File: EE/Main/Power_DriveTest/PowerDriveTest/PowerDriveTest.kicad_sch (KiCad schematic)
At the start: 31 parts, among them J8 Conn_01x02_Male, P1 USB_C_Plug_USB2.0, SW1 EG1206A, U2 LM3670MF-3.3, U4 MCP73832-2-OT, U5 MCP1640Cx-xCHY

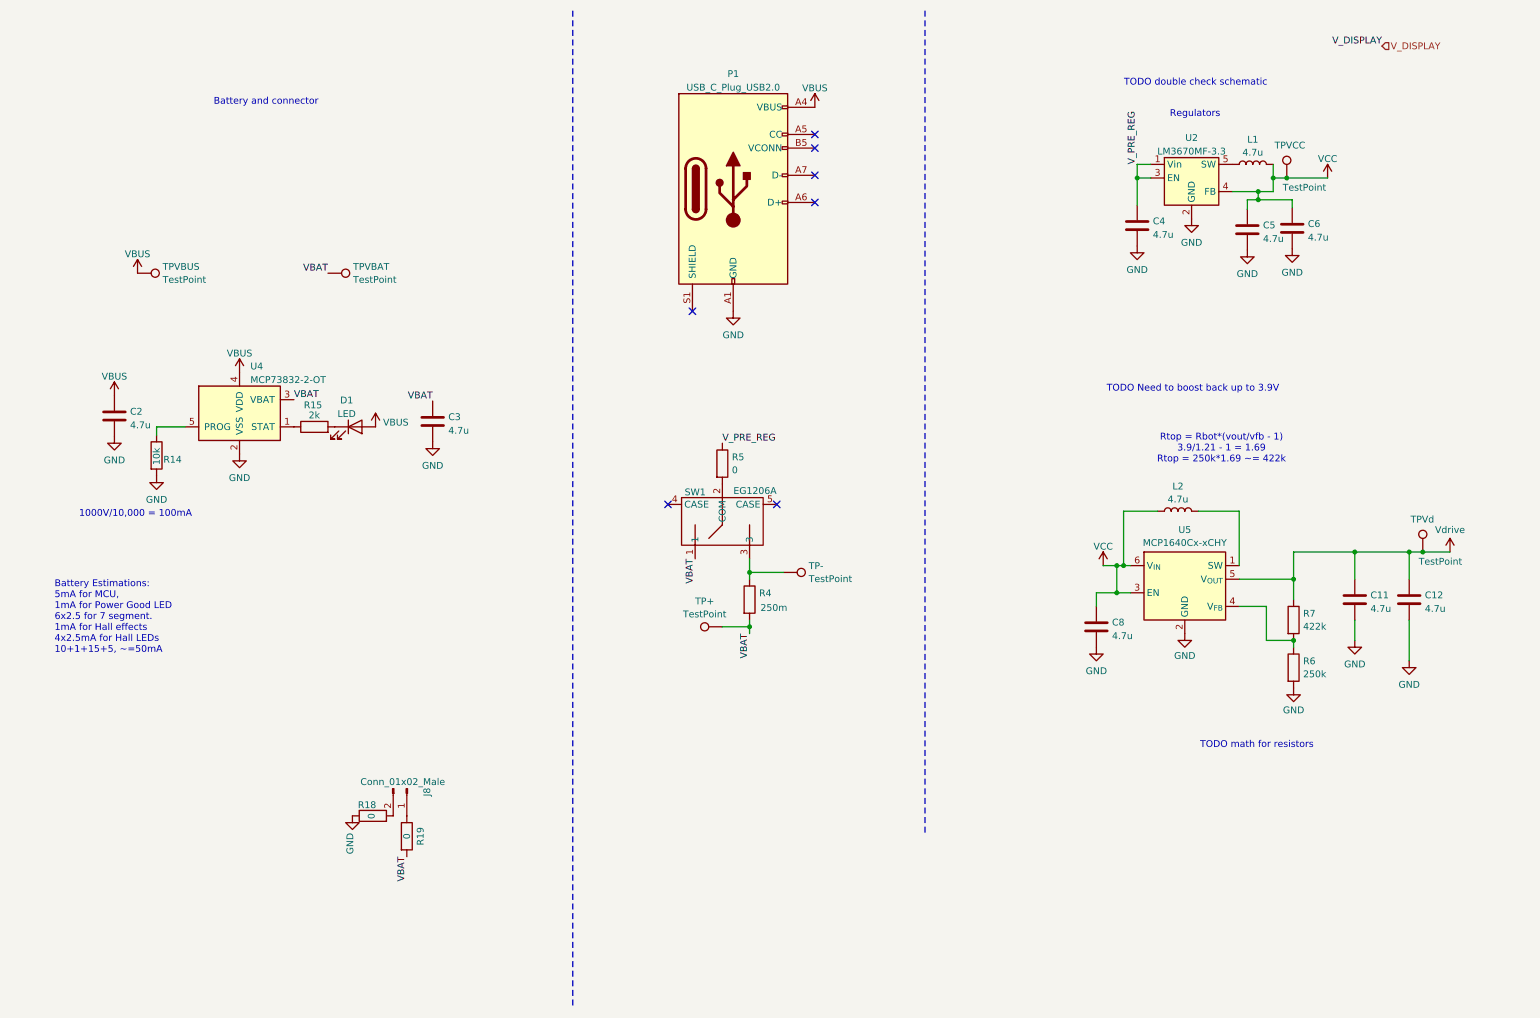
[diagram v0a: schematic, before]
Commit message: Sample Board for Power Supplies, Micro, And LED Driving.
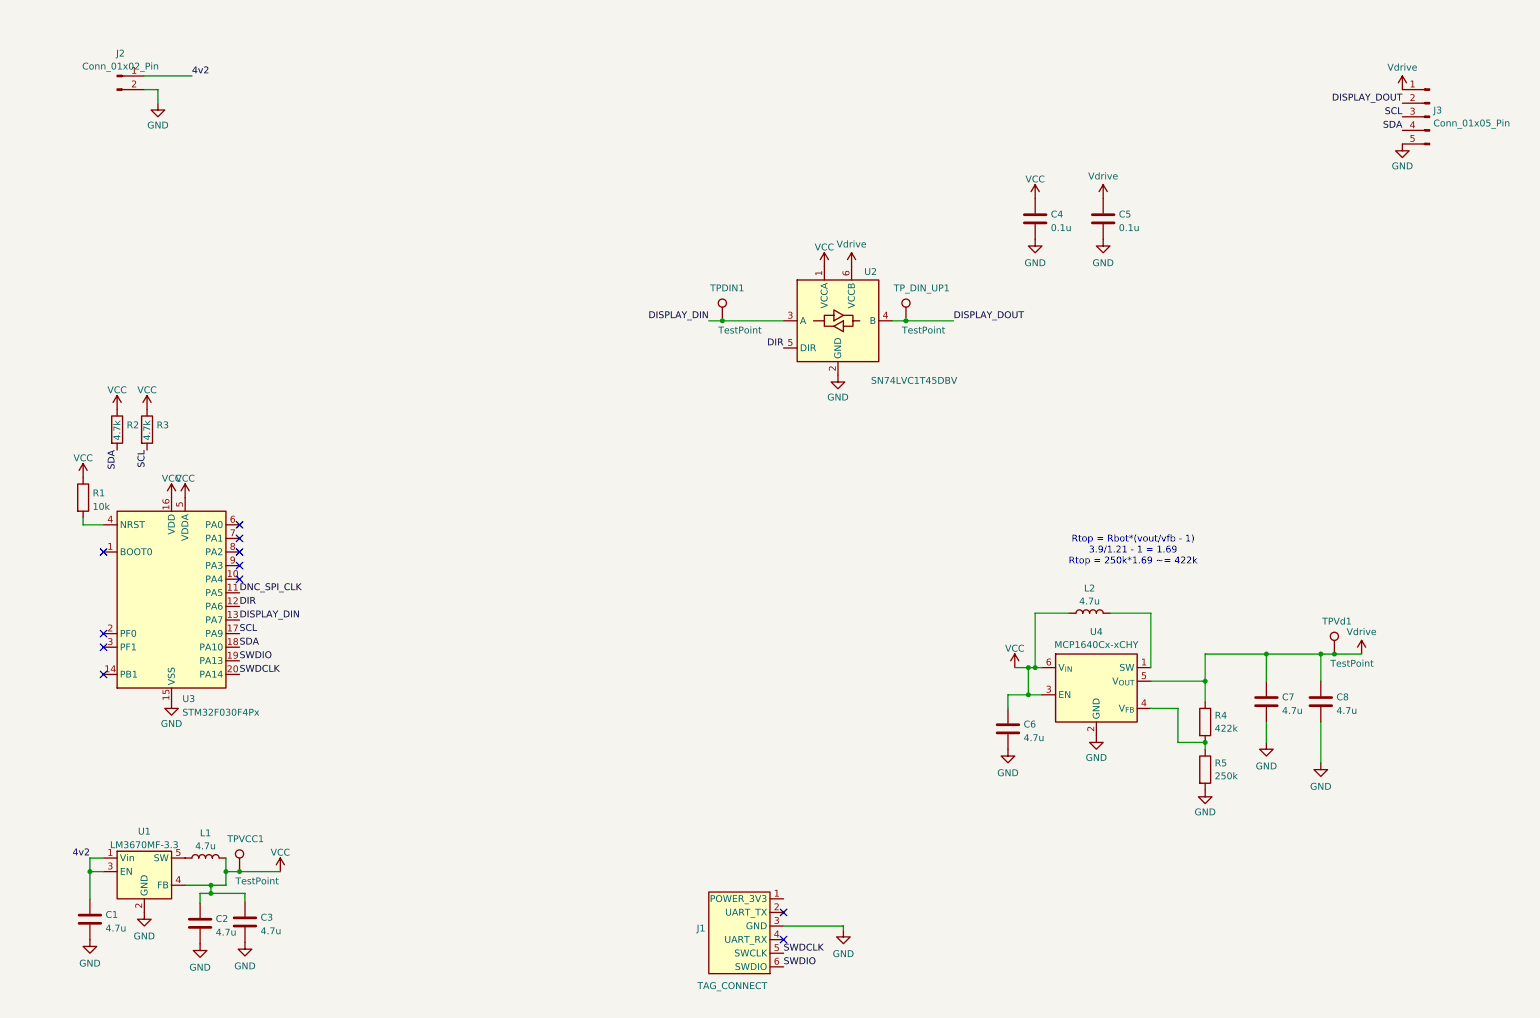
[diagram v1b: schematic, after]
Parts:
- removed C11, C12: 4.7u, Capacitor_SMD:C_0603_1608Metric, symbol Device:C
- removed D1: LED, LED_SMD:LED_0603_1608Metric, symbol Device:LED
- removed J8: Conn_01x02_Male, Connector_JST:JST_PH_B2B-PH-K_1x02_P2.00mm_Vertical, symbol Connector:Conn_01x02_Male
- removed P1: USB_C_Plug_USB2.0, Connector_USB:USB_C_Receptacle_GCT_USB4085, symbol Connector:USB_C_Plug_USB2.0
- removed R14: 10k, Resistor_SMD:R_0402_1005Metric, symbol Device:R
- removed R15: 2k, Resistor_SMD:R_0402_1005Metric, symbol Device:R
- removed R18, R19: 0, Resistor_SMD:R_0402_1005Metric, symbol Device:R
- removed R6: 250k, symbol Device:R
- removed R7: 422k, symbol Device:R
- removed SW1: EG1206A, Library:EG1206A_EWI, symbol New_Library:EG1206A
- removed TP+, TP-, TPVBAT, TPVBUS, TPVCC, TPVd: TestPoint, TestPoint:TestPoint_Pad_1.5x1.5mm, symbol Connector:TestPoint
- removed U2: LM3670MF-3.3, Package_TO_SOT_SMD:TSOT-23-5, symbol Regulator_Switching:LM3670MF
- removed U4: MCP73832-2-OT, Package_TO_SOT_SMD:SOT-23-5, symbol Battery_Management:MCP73832-2-OT
- removed U5: MCP1640Cx-xCHY, Package_TO_SOT_SMD:SOT-23-6, symbol Regulator_Switching:MCP1640Cx-xCHY
- added C1, C7: 4.7u, Capacitor_SMD:C_0603_1608Metric, symbol Device:C
- added J1: TAG_CONNECT, Connector:Tag-Connect_TC2030-IDC-FP_2x03_P1.27mm_Vertical, symbol ACTempDisconnect:TAG_CONNECT
- added J2: Conn_01x02_Pin, Connector_PinHeader_2.54mm:PinHeader_1x02_P2.54mm_Vertical, symbol Connector:Conn_01x02_Pin
- added J3: Conn_01x05_Pin, Connector_PinHeader_2.54mm:PinHeader_1x05_P2.54mm_Vertical, symbol Connector:Conn_01x05_Pin
- added R1: 10k, Resistor_SMD:R_0402_1005Metric, symbol Device:R
- added R2, R3: 4.7k, Resistor_SMD:R_0402_1005Metric, symbol Device:R
- added TPDIN1, TPVCC1, TPVd1, TP_DIN_UP1: TestPoint, TestPoint:TestPoint_Pad_1.5x1.5mm, symbol Connector:TestPoint
- added U1: LM3670MF-3.3, Package_TO_SOT_SMD:TSOT-23-5, symbol Regulator_Switching:LM3670MF
- added U2: SN74LVC1T45DBV, Package_TO_SOT_SMD:SOT-23-6, symbol Logic_LevelTranslator:SN74LVC1T45DBV
- added U3: STM32F030F4Px, Package_SO:TSSOP-20_4.4x6.5mm_P0.65mm, symbol MCU_ST_STM32F0:STM32F030F4Px
- added U4: MCP1640Cx-xCHY, Package_TO_SOT_SMD:SOT-23-6, symbol Regulator_Switching:MCP1640Cx-xCHY
- C4, C5: value 4.7u -> 0.1u; footprint Capacitor_SMD:C_0603_1608Metric -> Capacitor_SMD:C_0402_1005Metric
- R4: value 250m -> 422k; footprint Resistor_SMD:R_0805_2012Metric -> Resistor_SMD:R_0402_1005Metric_Pad0.72x0.64mm_HandSolder
- R5: value 0 -> 250k
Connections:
- net VBUS is gone; now on net VCC: C2.1
- net GND: now also R5.2, C1.2, C7.2, J1.3 (GND), J2.2 (Pin_2), J3.5 (Pin_5), U1.2 (GND), U2.2 (GND), U3.15 (VSS), U4.2 (GND)
- net VCC: now also C3.1, C4.1, R1.1, R2.1, R3.1, TPVCC1.1, U1.4 (FB), U2.1 (VCCA), U3.16 (VDD), U3.5 (VDDA), U4.3 (EN), U4.6 (V_{IN}); no longer C5.1, C8.1
- net Vdrive: now also C5.1, C8.1, R4.1, C7.1, J3.1 (Pin_1), TPVd1.1, U2.6 (VCCB), U4.5 (V_{OUT})
- net at L2.2: now also U4.1 (SW)
- net at L1.1: now also U1.5 (SW)
- net VBAT: no longer names the net of R4.2
- net VBAT: now also R5.1, U4.4 (V_{FB}); no longer C3.1
- removed net V_PRE_REG: C4.1, R5.1
- new net: R1.2, U3.4 (NRST)
- new net 4v2: C1.1, J2.1 (Pin_1), U1.1 (Vin), U1.3 (EN)
- new net DIR: U2.5 (DIR), U3.12 (PA6)
- new net DISPLAY_DIN: TPDIN1.1, U2.3 (A), U3.13 (PA7)
- new net DISPLAY_DOUT: J3.2 (Pin_2), TP_DIN_UP1.1, U2.4 (B)
- new net DNC_SPI_CLK: U3.11 (PA5)
- new net SCL: J3.3 (Pin_3), R3.2, U3.17 (PA9)
- new net SDA: J3.4 (Pin_4), R2.2, U3.18 (PA10)
- new net SWDCLK: J1.5 (SWCLK), U3.20 (PA14)
- new net SWDIO: J1.6 (SWDIO), U3.19 (PA13)
- no-connect marks 7 -> 11
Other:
- note removed: "1000V/10,000 = 100mA"
- note removed: "Battery Estimations: 5mA for MCU, 1mA for Power Good LED 6x2.5 for 7 segment. 1mA for Hall effects 4x2.5mA for Hall LEDs 10+1+15+5, ~=50mA"
- note removed: "Battery and connector"
- note removed: "Regulators"
- note removed: "TODO Need to boost back up to 3.9V"
- note removed: "TODO double check schematic"
- note removed: "TODO math for resistors"

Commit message: New Power Board off to mfging
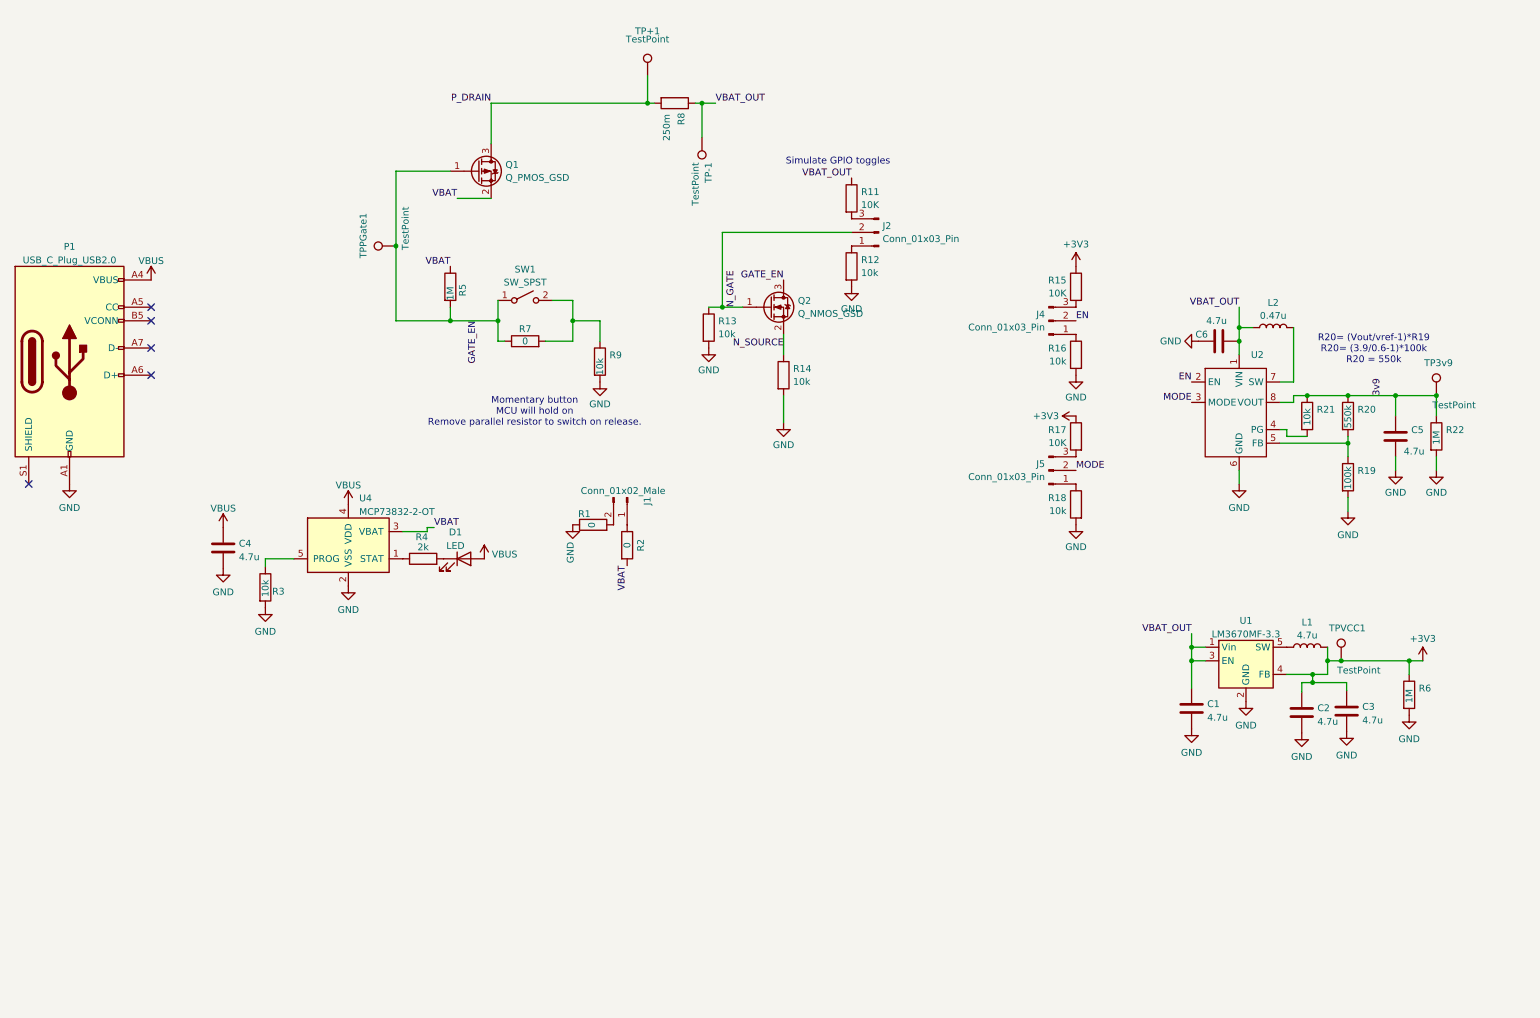
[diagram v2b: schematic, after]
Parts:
- removed C7, C8: 4.7u, Capacitor_SMD:C_0603_1608Metric, symbol Device:C
- removed J1: TAG_CONNECT, Connector:Tag-Connect_TC2030-IDC-FP_2x03_P1.27mm_Vertical, symbol ACTempDisconnect:TAG_CONNECT
- removed J2: Conn_01x02_Pin, Connector_PinHeader_2.54mm:PinHeader_1x02_P2.54mm_Vertical, symbol Connector:Conn_01x02_Pin
- removed J3: Conn_01x05_Pin, Connector_PinHeader_2.54mm:PinHeader_1x05_P2.54mm_Vertical, symbol Connector:Conn_01x05_Pin
- removed TPDIN1, TPVd1, TP_DIN_UP1: TestPoint, TestPoint:TestPoint_Pad_1.5x1.5mm, symbol Connector:TestPoint
- removed U2: SN74LVC1T45DBV, Package_TO_SOT_SMD:SOT-23-6, symbol Logic_LevelTranslator:SN74LVC1T45DBV
- removed U3: STM32F030F4Px, Package_SO:TSSOP-20_4.4x6.5mm_P0.65mm, symbol MCU_ST_STM32F0:STM32F030F4Px
- removed U4: MCP1640Cx-xCHY, Package_TO_SOT_SMD:SOT-23-6, symbol Regulator_Switching:MCP1640Cx-xCHY
- added D1: LED, LED_SMD:LED_0603_1608Metric, symbol Device:LED
- added J1: Conn_01x02_Male, Connector_JST:JST_PH_B2B-PH-K_1x02_P2.00mm_Vertical, symbol Connector:Conn_01x02_Male
- added J2, J4, J5: Conn_01x03_Pin, Connector_PinHeader_2.54mm:PinHeader_1x03_P2.54mm_Vertical, symbol Connector:Conn_01x03_Pin
- added P1: USB_C_Plug_USB2.0, Connector_USB:USB_C_Receptacle_GCT_USB4085, symbol Connector:USB_C_Plug_USB2.0
- added Q1: Q_PMOS_GSD, Package_TO_SOT_SMD:SOT-23, symbol Device:Q_PMOS_GSD
- added Q2: Q_NMOS_GSD, Package_TO_SOT_SMD:SOT-23, symbol Device:Q_NMOS_GSD
- added R11, R15, R17: 10K, Resistor_SMD:R_0402_1005Metric, symbol Device:R
- added R12, R13, R14, R16, R18, R21, R9: 10k, Resistor_SMD:R_0402_1005Metric, symbol Device:R
- added R19: 100k, Resistor_SMD:R_0402_1005Metric, symbol Device:R
- added R20: 550k, Resistor_SMD:R_0402_1005Metric, symbol Device:R
- added R22, R6: 1M, Resistor_SMD:R_0402_1005Metric, symbol Device:R
- added R7: 0, Resistor_SMD:R_0402_1005Metric, symbol Device:R
- added R8: 250m, Resistor_SMD:R_0805_2012Metric, symbol Device:R
- added SW1: SW_SPST, Button_Switch_SMD:SW_Tactile_SPST_NO_Straight_CK_PTS636Sx25SMTRLFS, symbol Switch:SW_SPST
- added TP+1, TP-1, TP3v9, TPPGate1: TestPoint, TestPoint:TestPoint_Pad_1.5x1.5mm, symbol Connector:TestPoint
- added U2: ~, Package_TO_SOT_SMD:SOT-583-8, symbol library:TPS61033
- added U4: MCP73832-2-OT, Package_TO_SOT_SMD:SOT-23-5, symbol Battery_Management:MCP73832-2-OT
- C4, C5: value 0.1u -> 4.7u; footprint Capacitor_SMD:C_0402_1005Metric -> Capacitor_SMD:C_0603_1608Metric
- L2: value 4.7u -> 0.47u; P/N 74479775222A -> (none)
- R1: value 10k -> 0
- R2: value 4.7k -> 0
- R3: value 4.7k -> 10k
- R4: value 422k -> 2k; footprint Resistor_SMD:R_0402_1005Metric_Pad0.72x0.64mm_HandSolder -> Resistor_SMD:R_0402_1005Metric
- R5: value 250k -> 1M; footprint Resistor_SMD:R_0402_1005Metric_Pad0.72x0.64mm_HandSolder -> Resistor_SMD:R_0402_1005Metric
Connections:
- net SCL is gone; now on net GND: R3.2
- net GND: now also C6.1, R1.1, P1.A1 (GND), P1.A12 (GND), P1.B1 (GND), P1.B12 (GND), R12.2, R13.2, R14.2, R16.2, R18.2, R19.2, R22.2, R6.2, R9.2, U2.6 (GND), U4.2 (VSS); no longer C6.2, R5.2
- net at R4.2: now also D1.1 (K); no longer R5.1
- net at R1.2: now also J1.2 (Pin_2)
- net at L2.2: now also U2.7 (SW)
- net 4v2 renamed VBAT_OUT
- net VBAT_OUT: now also C6.2, L2.1, R11.1, R8.1, TP-1.1, U2.1 (VIN)
- net SDA renamed VBAT
- net VBAT: now also R5.1, Q1.2 (S), U4.3 (VBAT)
- removed net VCC: C2.1, C3.1, C4.1, C6.1, L1.2, L2.1, R1.1, R2.1, R3.1, TPVCC1.1, U1.4 (FB)
- net Vdrive: no longer names the net of R4.1
- net Vdrive: now also U4.1 (STAT); no longer C5.1
- new net: J4.1 (Pin_1), R16.1
- new net: R3.1, U4.5 (PROG)
- new net: J5.3 (Pin_3), R17.2
- new net: J5.1 (Pin_1), R18.1
- new net: J2.1 (Pin_1), R12.1
- new net: J2.3 (Pin_3), R11.2
- new net: R7.2, R9.1, SW1.2 (B)
- new net: R21.2, U2.4 (PG)
- new net: J4.3 (Pin_3), R15.2
- new net: R19.1, R20.2, U2.5 (FB)
- new net: J1.1 (Pin_1), R2.1
- new net +3V3: C2.1, C3.1, L1.2, R15.1, R17.1, R6.1, TPVCC1.1, U1.4 (FB)
- new net 3v9: C5.1, R20.1, R21.1, R22.1, TP3v9.1, U2.8 (VOUT)
- new net EN: J4.2 (Pin_2), U2.2 (EN)
- new net GATE_EN: Q1.1 (G), Q2.3 (D), R5.2, R7.1, SW1.1 (A), TPPGate1.1
- new net MODE: J5.2 (Pin_2), U2.3 (MODE)
- new net N_GATE: J2.2 (Pin_2), Q2.1 (G), R13.1
- new net N_SOURCE: Q2.2 (S), R14.1
- new net P_DRAIN: Q1.3 (D), R8.2, TP+1.1
- new net VBUS: C4.1, D1.2 (A), P1.A4 (VBUS), P1.A9 (VBUS), P1.B4 (VBUS), P1.B9 (VBUS), U4.4 (VDD)
- no-connect marks 11 -> 5
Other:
- note added: "Momentary button MCU will hold on Remove parallel resistor to switch on release."
- note added: "R20= (Vout/vref-1)*R19 R20= (3.9/0.6-1)*100k R20 = 550k"
- note added: "Simulate GPIO toggles"
- note removed: "Rtop = Rbot*(vout/vfb - 1) 3.9/1.21 - 1 = 1.69 Rtop = 250k*1.69 ~= 422k"
- moved on the sheet: C1, C2, C3, L1, TPVCC1, U1
